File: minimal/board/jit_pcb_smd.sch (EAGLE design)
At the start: 44 parts, among them Q2 MC-306 32.7680K-A0, U1 FT232RL

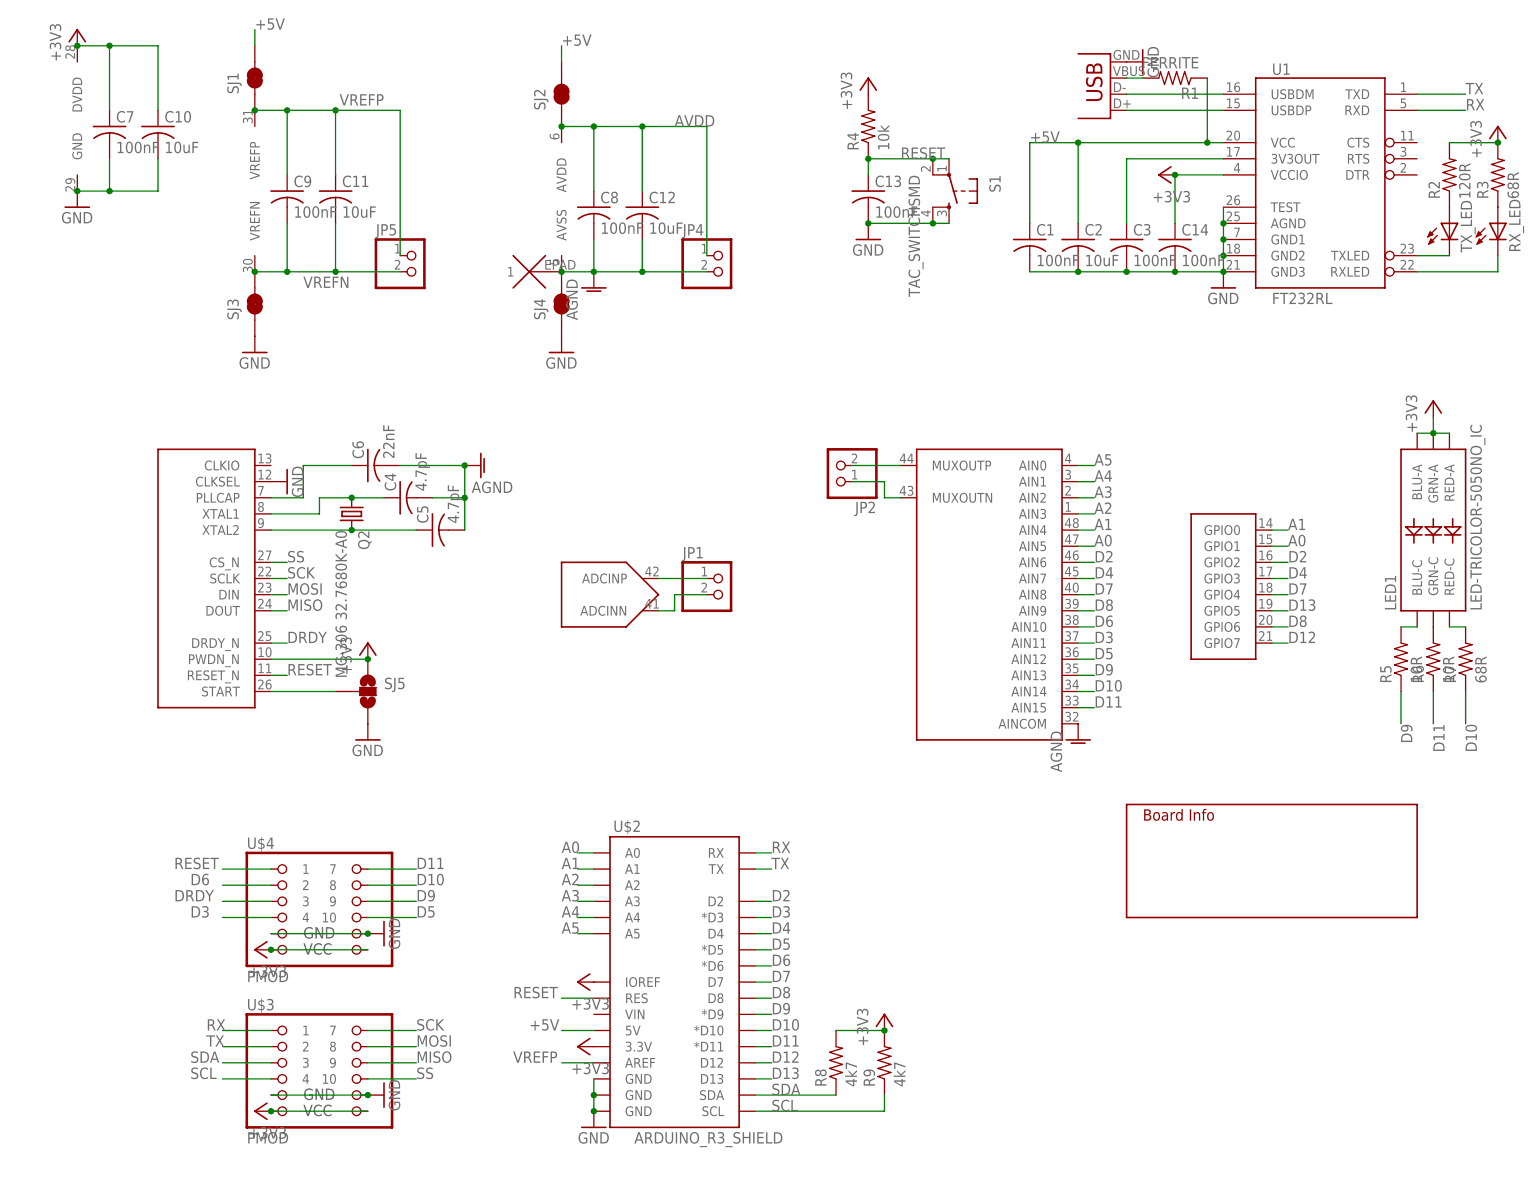
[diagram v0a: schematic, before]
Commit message: Adding all boards for minimal and carrier board with MKL05Z32
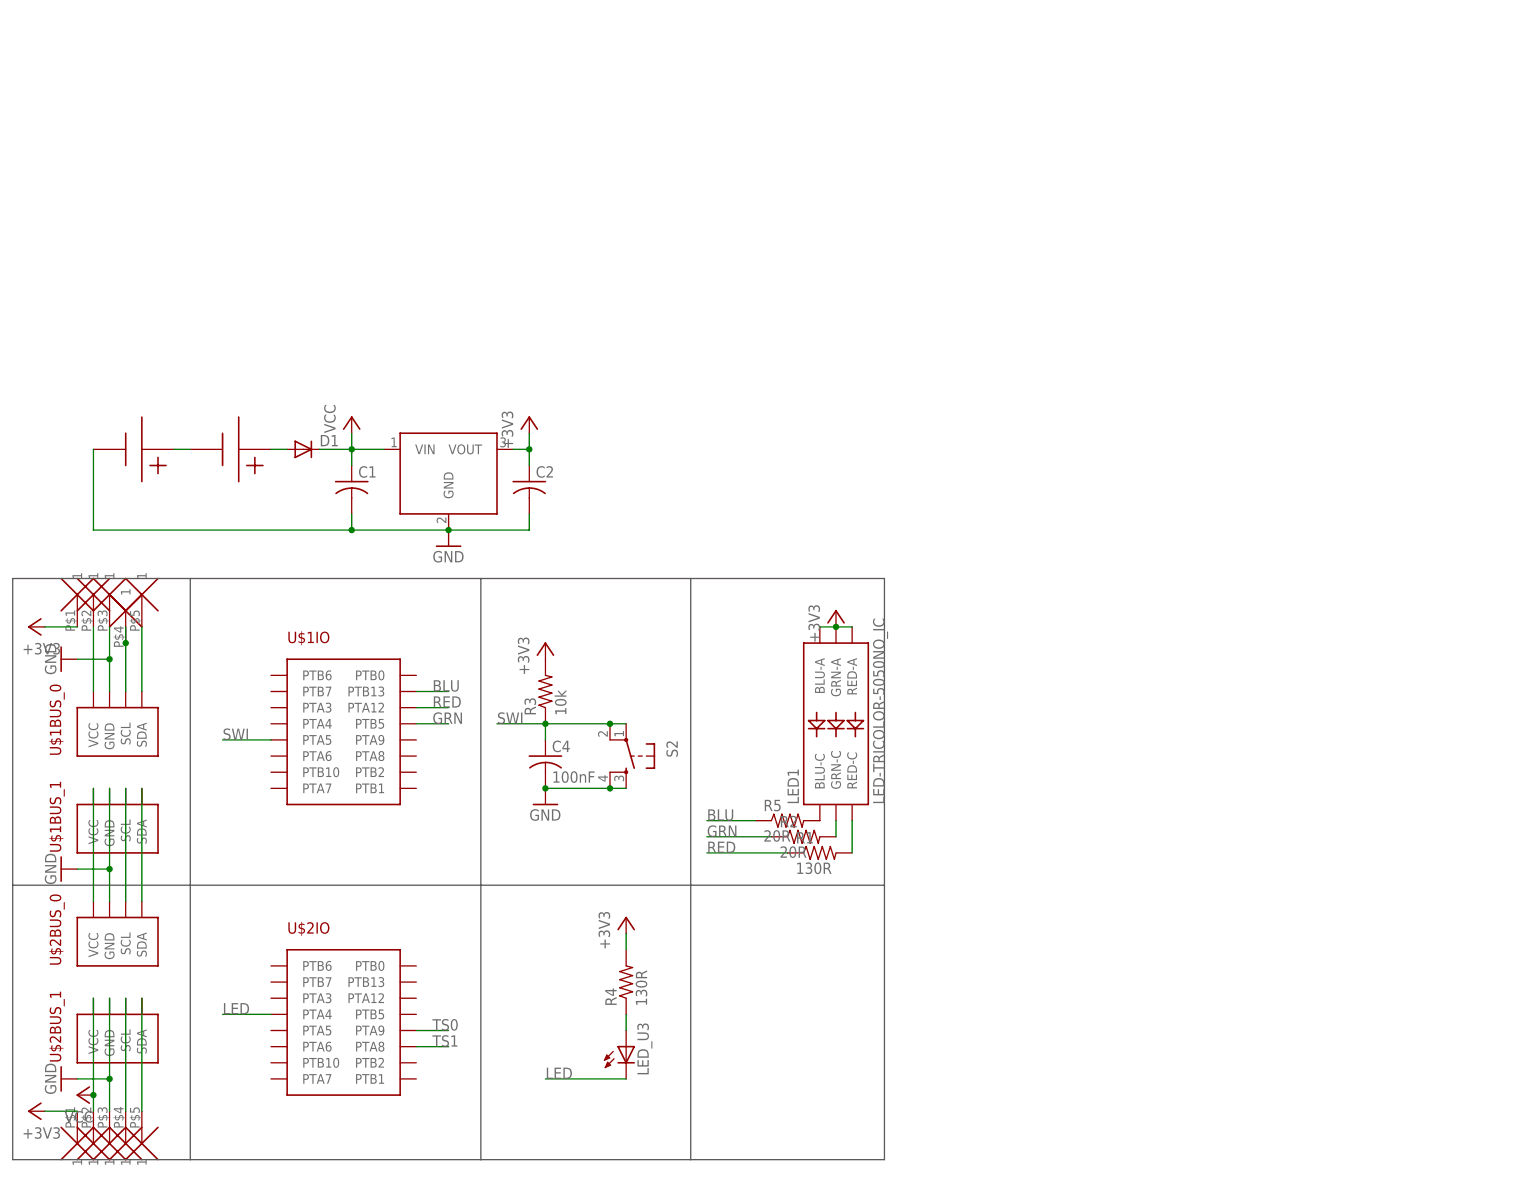
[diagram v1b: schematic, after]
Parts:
- removed C10, C11, C12: 10uF, rcl:C-USC0603
- removed C13, C14, C3, C7, C8, C9: 100nF, rcl:C-USC0603
- removed C5: 4.7pF, rcl:C-USC0603
- removed C6: 22nF, rcl:C-USC0603
- removed JP1, JP2, JP4, JP5: (no value), pinhead:PINHD-1X2
- removed JP3: USBSMD, SparkFun-Connectors:USBSMD
- removed Q2: MC-306 32.7680K-A0, crystal:MC-306
- removed R6: 10R, rcl:R-US_R0603
- removed R7: 68R, rcl:R-US_R0603
- removed R8, R9: 4k7, rcl:R-US_R0603
- removed RX_LED, TX_LED: (no value), led:LEDCHIPLED_0603
- removed S1: TAC_SWITCHSMD, SparkFun-Electromechanical:TAC_SWITCHSMD
- removed SJ1, SJ2, SJ3, SJ4: JUMPER-PAD-2-NC_BY_TRACE, SparkFun-Passives:JUMPER-PAD-2-NC_BY_TRACE
- removed SJ5: JUMPER-PAD-3-NOYES_SILK, SparkFun-Passives:JUMPER-PAD-3-NOYES_SILK
- removed U1: FT232RL, SparkFun-DigitalIC:FT232RL-BASICSSOP
- added D1: (no value), diode:DIODE-SMC
- added LED_U3: (no value), led:LEDCHIP-LED0805
- added S2: (no value), SparkFun-Electromechanical:TAC_SWITCHSMD
- added U$6, U$7: 1X5_SMD, modular_robotics:1X5_SMD
- C1: value 100nF -> (none); device rcl:C-USC0603 -> rcl:C-USC0805
- C2: value 10uF -> (none); device rcl:C-USC0603 -> rcl:C-USC0805
- C4: value 4.7pF -> 100nF; device rcl:C-USC0603 -> rcl:C-USC0805
- R1: value FERRITE -> 130R; device rcl:R-US_R0603 -> rcl:R-US_R0805
- R2: value 120R -> 20R; device rcl:R-US_R0603 -> rcl:R-US_R0805
- R3: value 68R -> 10k; device rcl:R-US_R0603 -> rcl:R-US_R0805
- R4: value 10k -> 130R; device rcl:R-US_R0603 -> rcl:R-US_R0805
- R5: value 10R -> 20R; device rcl:R-US_R0603 -> rcl:R-US_R0805
- U$1: value ADS1258 -> MODROB_CARRIER-SMD; device modular_robotics:ADS1258 -> modular_robotics:MODROB_CARRIER-SMD
- U$2: value ARDUINO_R3_SHIELD -> MODROB_CARRIER-SMD; device SparkFun-Boards:ARDUINO_R3_SHIELD -> modular_robotics:MODROB_CARRIER-SMD
- U$3, U$4: value PMOD -> CR3023; device modular_robotics:PMOD -> modular_robotics:CR3023
- U$5: value INFO -> TC1262; device modular_robotics:INFO -> modular_robotics:TC1262; AUTHOR Austin Buchan -> (none); DATE Nov 18, 2014 -> (none); DESIGN Zedboard Arduino Adapter -> (none); ORGANIZATION UC Berkeley ASPIRE -> (none); REVISION r0.1 -> (none)
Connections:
- removed net +5V: C1.1, C2.1, R1.1, SJ1.2, SJ2.2, U$2.5V, U1.VCC
- removed net A0: U$1GPIO.GPIO1, U$1MUX.AIN5, U$2.A0
- removed net A1: U$1GPIO.GPIO0, U$1MUX.AIN4, U$2.A1
- removed net A2: U$1MUX.AIN3, U$2.A2
- removed net A3: U$1MUX.AIN2, U$2.A3
- removed net A4: U$1MUX.AIN1, U$2.A4
- removed net A5: U$1MUX.AIN0, U$2.A5
- removed net ADCN: JP1.2, U$1ADC.ADCINN
- removed net ADCP: JP1.1, U$1ADC.ADCINP
- removed net AGND: C12.2, C4.2, C5.2, C6.2, C8.2, JP4.2, SJ4.2, U$1AVDD-AVSS.AVSS, U$1EPAD.1, U$1MUX.AINCOM
- removed net AVDD: C12.1, C8.1, JP4.1, SJ2.1, U$1AVDD-AVSS.AVDD
- removed net D10: R7.1, U$1MUX.AIN14, U$2.*D10, U$4.8
- removed net D11: R6.1, U$1MUX.AIN15, U$2.*D11, U$4.7
- removed net D12: U$1GPIO.GPIO7, U$2.D12
- removed net D13: U$1GPIO.GPIO5, U$2.D13
- removed net D2: U$1GPIO.GPIO2, U$1MUX.AIN6, U$2.D2
- removed net D3: U$1MUX.AIN11, U$2.*D3, U$4.4
- removed net D4: U$1GPIO.GPIO3, U$1MUX.AIN7, U$2.D4
- removed net D5: U$1MUX.AIN12, U$2.*D5, U$4.10
- removed net D6: U$1MUX.AIN10, U$2.*D6, U$4.2
- removed net D7: U$1GPIO.GPIO4, U$1MUX.AIN8, U$2.D7
- removed net D8: U$1GPIO.GPIO6, U$1MUX.AIN9, U$2.D8
- removed net D9: R5.1, U$1MUX.AIN13, U$2.*D9, U$4.9
- removed net DRDY: U$1CTRL.DRDY_N, U$4.3
- removed net MISO: U$1CTRL.DOUT, U$3.9
- removed net MOSI: U$1CTRL.DIN, U$3.8
- removed net MUXN: JP2.1, U$1MUX.MUXOUTN
- removed net MUXP: JP2.2, U$1MUX.MUXOUTP
- removed net N$18: LED1.GRN-C, R6.2
- removed net N$21: LED1.RED-C, R7.2
- removed net N$6: SJ5.2, U$1CTRL.START
- removed net RESET: C13.1, R4.1, S1.1, S1.2, U$1CTRL.RESET_N, U$2.RES, U$4.1
- removed net RX: U$2.RX, U$3.1, U1.RXD
- removed net SCK: U$1CTRL.SCLK, U$3.7
- removed net SCL: R9.1, U$2.SCL, U$3.4
- removed net SDA: R8.1, U$2.SDA, U$3.3
- removed net SS: U$1CTRL.CS_N, U$3.10
- removed net TX: U$2.TX, U$3.2, U1.TXD
- removed net VREFN: C11.2, C9.2, JP5.2, SJ3.2, U$1VREFN-VREFP.VREFN
- removed net VREFP: C11.1, C9.1, JP5.1, SJ1.1, U$1VREFN-VREFP.VREFP, U$2.AREF
- new net BLU: R5.1, U$1IO.PTB13
- new net GRN: R2.1, U$1IO.PTB5
- new net LED: LED_U3.C, U$2IO.PTA4
- new net N$10: U$2BUS_1.SDA, U$6G$5.1
- new net N$12: LED1.RED-C, R1.2
- new net RED: R1.1, U$1IO.PTA12
- new net SWI: C4.1, R3.1, S2.1, S2.2, U$1IO.PTA5
- new net TS0: U$2IO.PTA9
- new net TS1: U$2IO.PTA8
- new net VCC: C1.1, D1.C, U$2BUS_1.VCC, U$5.VIN, U$6G$2.1
- net +3V3: now also C2.1, U$5.VOUT, U$6G$1.1, U$7G$1.1; no longer C10.1, C14.1, C7.1, R2.2, R8.2, R9.2, SJ5.1, U$1CTRL.PWDN_N, U$1GND-DVDD.DVDD, U$2.3.3V, U$2.IOREF, U$3.12, U$3.6, U$4.12, U$4.6, U1.VCCIO
- net GND: now also C4.2, S2.3, S2.4, U$1BUS_0.GND, U$1BUS_1.GND, U$2BUS_0.GND, U$2BUS_1.GND, U$3.-, U$5.GND, U$6G$3.1, U$7G$3.1; no longer C10.2, C13.2, C14.2, C3.2, C7.2, JP3.GND, S1.3, S1.4, SJ3.1, SJ4.1, SJ5.3, U$1CTRL.CLKSEL, U$1GND-DVDD.GND, U$2.GND@0, U$2.GND@1, U$2.GND@2, U$3.11, U$3.5, U$4.11, U$4.5, U1.AGND, U1.GND1, U1.GND2, U1.GND3, U1.TEST
- net N$1: now also U$1BUS_0.VCC, U$7G$2.1; no longer JP3.D+, U1.USBDP
- net N$13: now also U$3.+, U$4.-; no longer C6.1, U$1CTRL.PLLCAP
- net N$14: now also LED1.GRN-C, R2.2; no longer C4.1, Q2.1, U$1CTRL.XTAL1
- net N$15: now also D1.A, U$4.+; no longer C5.1, Q2.2, U$1CTRL.XTAL2
- net N$2: now also U$1BUS_1.VCC, U$2BUS_0.VCC; no longer JP3.D-, U1.USBDM
- net N$3: now also U$1BUS_0.SCL, U$7G$4.1; no longer R2.1, TX_LED.A
- net N$4: now also LED_U3.A, R4.1; no longer R3.1, RX_LED.A
- net N$5: now also U$1BUS_0.SDA, U$7G$5.1; no longer C3.1, U1.3V3OUT
- net N$7: now also U$1BUS_1.SCL, U$2BUS_0.SCL; no longer JP3.VBUS, R1.2
- net N$8: now also U$1BUS_1.SDA, U$2BUS_0.SDA; no longer TX_LED.C, U1.TXLED
- net N$9: now also U$2BUS_1.SCL, U$6G$4.1; no longer RX_LED.C, U1.RXLED
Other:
- moved on the sheet: C1, C2, C4, LED1, R1, R2, R3, R4, R5
